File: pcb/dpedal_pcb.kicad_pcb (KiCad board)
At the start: 2 copper layers, 134 x 68 mm, 7 parts, among them SW1 SW_Push, SW2 SW_Push, SW3 SW_Push, SW4 SW_Push, SW5 SW_Push, SW6 SW_Push

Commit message: board redesign
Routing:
- net Net-(A1-GPIO3): track 24.2 -> 0.00 mm
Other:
- board size 134 x 68 mm -> 126.5 x 55.5 mm

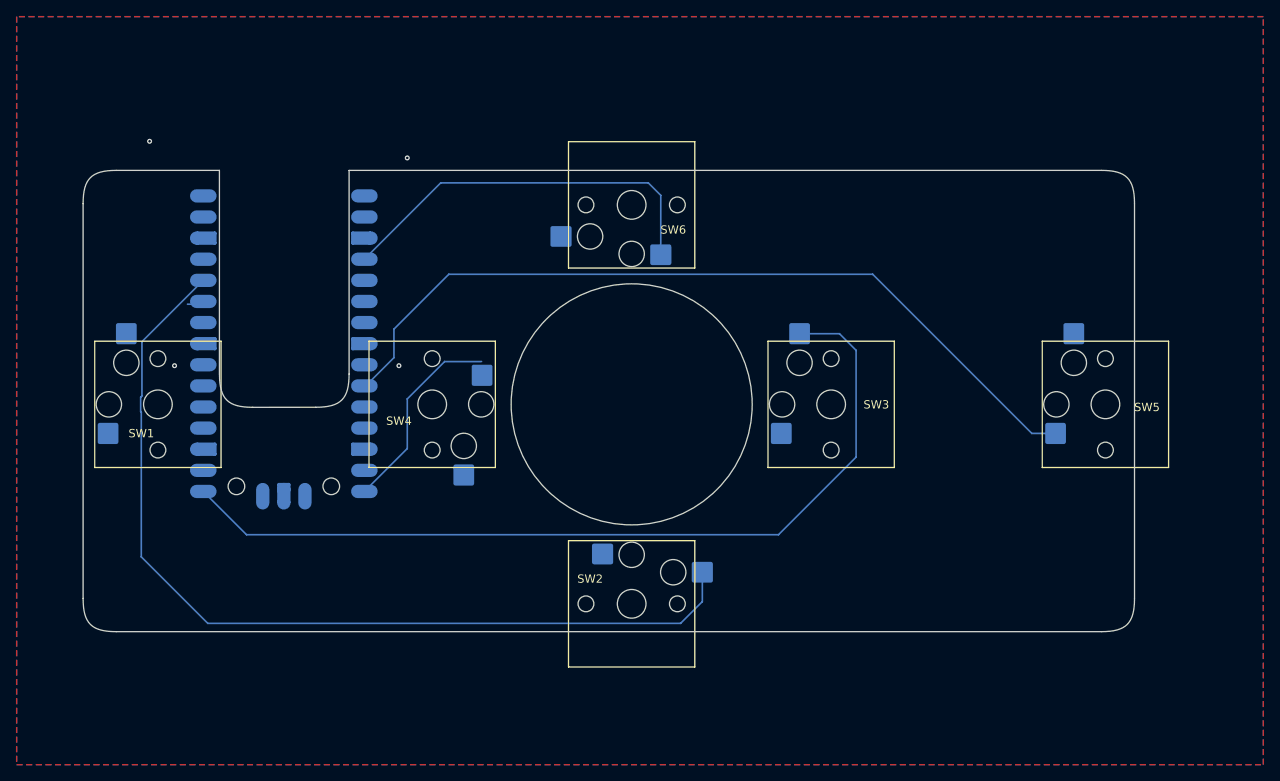
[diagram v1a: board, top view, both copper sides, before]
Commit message: add step file to kicad export script
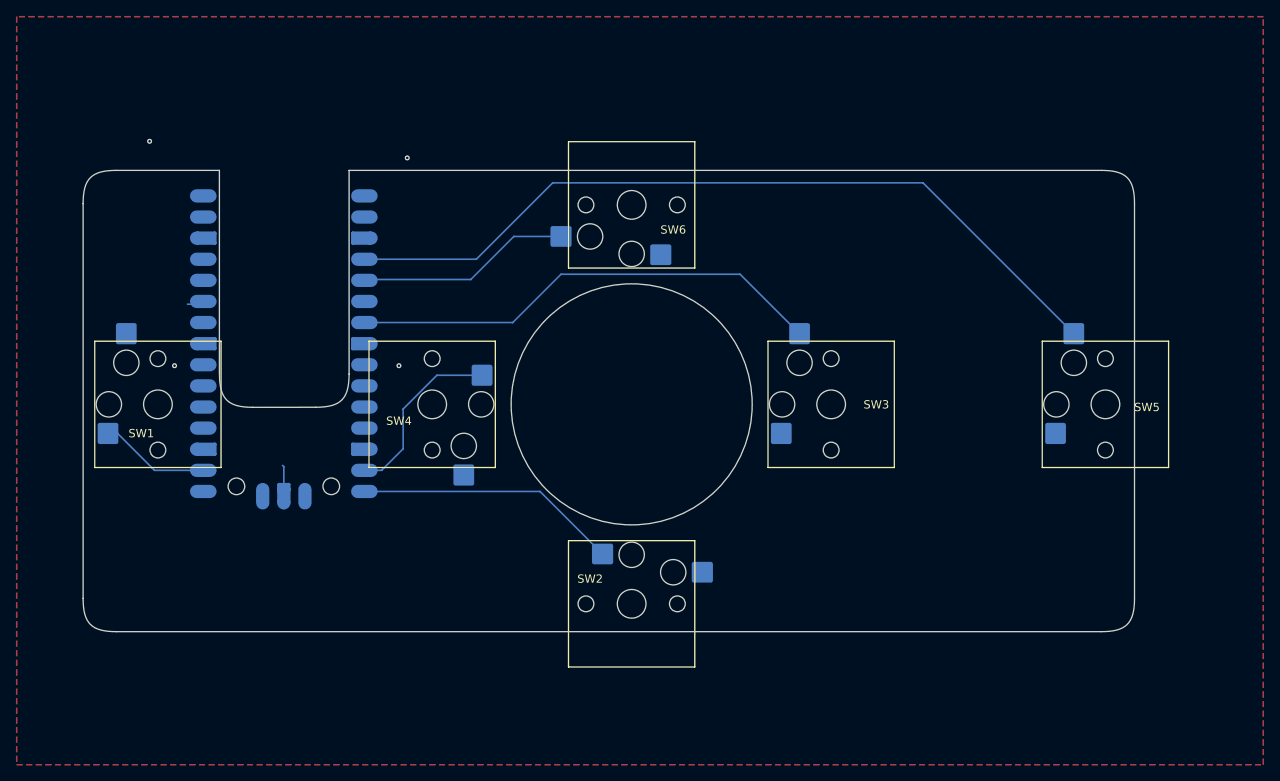
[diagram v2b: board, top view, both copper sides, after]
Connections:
- A1 pad 10: Net-(A1-GPIO7) -> unconnected-(A1-GPIO7-Pad10)
- A1 pad 19: unconnected-(A1-GPIO14-Pad19) -> button_left
- A1 pad 20: Net-(A1-GPIO15) -> unconnected-(A1-GPIO15-Pad20)
- A1 pad 21: Net-(A1-GPIO16) -> dpad_down
- A1 pad 22: unconnected-(A1-GPIO17-Pad22) -> dpad_left
- A1 pad 26: Net-(A1-GPIO20) -> unconnected-(A1-GPIO20-Pad26)
- A1 pad 29: unconnected-(A1-GPIO22-Pad29) -> dpad_right
- A1 pad 31: unconnected-(A1-GPIO26_ADC0-Pad31) -> dpad_up
- A1 pad 32: Net-(A1-GPIO27_ADC1) -> button_right
- SW1 pad 1: GND -> button_left
- SW1 pad 2: Net-(A1-GPIO3) -> GND
- SW2 pad 1: GND -> dpad_down
- SW2 pad 2: Net-(A1-GPIO7) -> GND
- SW3 pad 2: Net-(A1-GPIO15) -> dpad_right
- SW4 pad 1: Net-(A1-GPIO16) -> dpad_left
- SW5 pad 1: Net-(A1-GPIO20) -> GND
- SW5 pad 2: GND -> button_right
- SW6 pad 1: Net-(A1-GPIO27_ADC1) -> GND
- SW6 pad 2: GND -> dpad_up
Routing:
- net Net-(A1-GPIO7): track 111.9 -> 0.00 mm
- net Net-(A1-GPIO15): track 105.0 -> 0.00 mm
- net Net-(A1-GPIO20): track 98.5 -> 0.00 mm
- net button_right: track 0.00 -> 97.0 mm
- net dpad_right: track 0.00 -> 57.7 mm
- net Net-(A1-GPIO27_ADC1): track 47.2 -> 0.00 mm
- net dpad_down: track 0.00 -> 31.8 mm
- net dpad_up: track 0.00 -> 25.8 mm
- net Net-(A1-GPIO16): track 24.1 -> 0.00 mm
- net dpad_left: track 0.00 -> 21.7 mm
- net button_left: track 0.00 -> 13.3 mm
- net GND: track 0.00 -> 2.96 mm

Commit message: fix erc/drc
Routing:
- net unconnected-(A1-GPIO8-Pad11): track 2.06 -> 0.00 mm
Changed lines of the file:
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@@
 		(tags "module usb pcb swd")
 		(property "Reference" "A1"
-			(at -14.69 14 0)
+			(at -13.85 7 0)
 			(unlocked yes)
 			(layer "B.SilkS")
@@
 			(net 20 "unconnected-(A1-GPIO4-Pad6)")
 			(pinfunction "GPIO4")
-			(pintype "bidirectional")
+			(pintype "bidirectional+no_connect")
 		)
 		(pad "7" smd roundrect
@@
 			(net 18 "unconnected-(A1-GPIO5-Pad7)")
 			(pinfunction "GPIO5")
-			(pintype "bidirectional")
+			(pintype "bidirectional+no_connect")
 		)
 		(pad "8" smd custom
@@
 			(net 26 "unconnected-(A1-GPIO6-Pad9)")
 			(pinfunction "GPIO6")
-			(pintype "bidirectional")
+			(pintype "bidirectional+no_connect")
 		)
 		(pad "10" smd roundrect
@@
 			(net 7 "unconnected-(A1-GPIO7-Pad10)")
 			(pinfunction "GPIO7")
-			(pintype "bidirectional")
+			(pintype "bidirectional+no_connect")
 		)
 		(pad "11" smd roundrect
@@
 			(net 14 "unconnected-(A1-GPIO8-Pad11)")
 			(pinfunction "GPIO8")
-			(pintype "bidirectional")
+			(pintype "bidirectional+no_connect")
 		)
 		(pad "12" smd roundrect
@@
 			(net 4 "unconnected-(A1-GPIO9-Pad12)")
 			(pinfunction "GPIO9")
-			(pintype "bidirectional")
+			(pintype "bidirectional+no_connect")
 		)
 		(pad "13" smd custom
@@
 			(net 23 "unconnected-(A1-GPIO10-Pad14)")
 			(pinfunction "GPIO10")
-			(pintype "bidirectional")
+			(pintype "bidirectional+no_connect")
 		)
 		(pad "15" smd roundrect
@@
 			(net 19 "unconnected-(A1-GPIO11-Pad15)")
 			(pinfunction "GPIO11")
-			(pintype "bidirectional")
+			(pintype "bidirectional+no_connect")
 		)
 		(pad "16" smd roundrect
@@
 			(net 24 "unconnected-(A1-GPIO12-Pad16)")
 			(pinfunction "GPIO12")
-			(pintype "bidirectional")
+			(pintype "bidirectional+no_connect")
 		)
 		(pad "17" smd roundrect
@@
 			(net 25 "unconnected-(A1-GPIO13-Pad17)")
 			(pinfunction "GPIO13")
-			(pintype "bidirectional")
+			(pintype "bidirectional+no_connect")
 		)
 		(pad "18" smd custom
@@
 			(net 3 "unconnected-(A1-GPIO15-Pad20)")
 			(pinfunction "GPIO15")
-			(pintype "bidirectional")
+			(pintype "bidirectional+no_connect")
 		)
 		(pad "21" smd roundrect
@@
 			(net 6 "unconnected-(A1-GPIO18-Pad24)")
 			(pinfunction "GPIO18")
-			(pintype "bidirectional")
+			(pintype "bidirectional+no_connect")
 		)
 		(pad "25" smd roundrect
@@
 			(net 22 "unconnected-(A1-GPIO19-Pad25)")
 			(pinfunction "GPIO19")
-			(pintype "bidirectional")
+			(pintype "bidirectional+no_connect")
 		)
 		(pad "26" smd roundrect
@@
 			(net 8 "unconnected-(A1-GPIO20-Pad26)")
 			(pinfunction "GPIO20")
-			(pintype "bidirectional")
+			(pintype "bidirectional+no_connect")
 		)
 		(pad "27" smd roundrect
@@
 			(net 10 "unconnected-(A1-GPIO21-Pad27)")
 			(pinfunction "GPIO21")
-			(pintype "bidirectional")
+			(pintype "bidirectional+no_connect")
 		)
 		(pad "28" smd custom
@@
 			(net 21 "unconnected-(A1-RUN-Pad30)")
 			(pinfunction "RUN")
-			(pintype "passive")
+			(pintype "passive+no_connect")
 		)
 		(pad "31" smd roundrect
@@
 			(layers "B.Cu" "B.Mask")
 			(net 27 "GND")
-			(pinfunction "AGND")
+			(pinfunction "GND")
 			(pintype "power_out")
 			(options
@@
 			(net 2 "unconnected-(A1-GPIO28_ADC2-Pad34)")
 			(pinfunction "GPIO28_ADC2")
-			(pintype "bidirectional")
+			(pintype "bidirectional+no_connect")
 		)
 		(pad "35" smd roundrect
@@
 			(net 15 "unconnected-(A1-ADC_VREF-Pad35)")
 			(pinfunction "ADC_VREF")
-			(pintype "power_in")
+			(pintype "power_in+no_connect")
 		)
 		(pad "D1" smd roundrect
@@
 			(net 13 "unconnected-(A1-SWCLK-PadD1)")
 			(pinfunction "SWCLK")
-			(pintype "input")
+			(pintype "input+no_connect")
 		)
 		(pad "D2" smd custom
@@
 			(net 11 "unconnected-(A1-SWDIO-PadD3)")
 			(pinfunction "SWDIO")
-			(pintype "bidirectional")
+			(pintype "bidirectional+no_connect")
 		)
 		(group ""
@@
 	)
 	(segment
-		(start 115.62 124.6)
-		(end 113.560108 124.6)
-		(width 0.2)
-		(layer "B.Cu")
-		(net 14)
-	)
-	(segment
 		(start 147.645744 121.629403)
 		(end 134.940597 121.629403)
@@
 	)
 	(via
-		(at 140 107)
+		(at 143.5 114.5)
 		(size 0.6)
 		(drill 0.3)
@@
 	)
 	(via
-		(at 109 105)
+		(at 207 136)
 		(size 0.6)
 		(drill 0.3)
